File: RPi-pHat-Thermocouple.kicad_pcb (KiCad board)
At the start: 2 copper layers, 65 x 30 mm, 59 parts, among them J1 RPi_GPIO, J2 Barrel_Jack_Switch, P1 CONN_01X02, P2 CONN_01X02, P3 CONN_01X02, P6 CONN_01X03, Q1 NUD3124, Q2 BCM857BS, Q3 DMG2305UX, SW1 Write, U1 MAX31850K, U2 MAX31850K, U3 MAX31850K, U4 DS18S20, U5 AT24CS32, U6 LMZ21700, U7 MCP1754ST

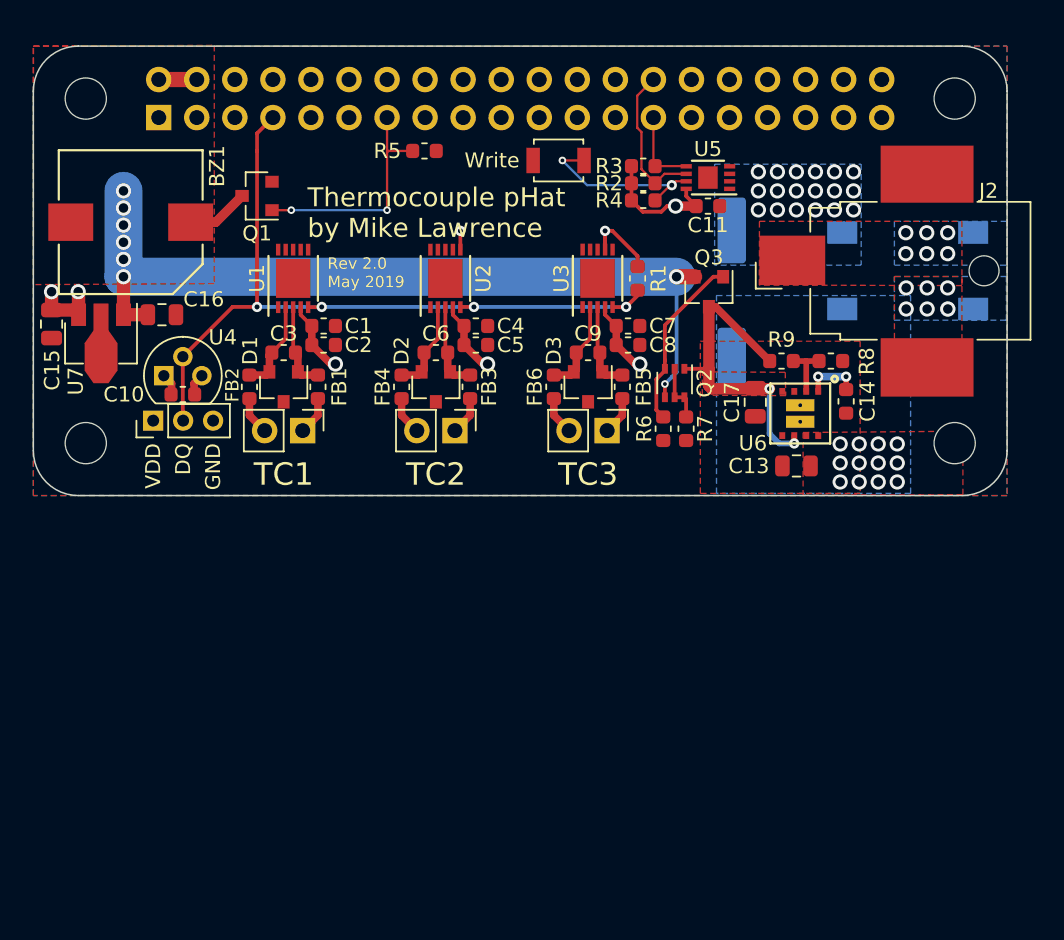
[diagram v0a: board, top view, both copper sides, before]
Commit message: Variation for generator monitoring application.
Remove buzzer and related; remove Pi Hat EEPROM.

Since the form factor is going to expand a bit beyond the Pi-Hat
specification to enable adding an isolated RS-232/TTL interface for
the Raspberry Pi serial port, we'll remove the parts that are not needed
for the generator-targeted application.
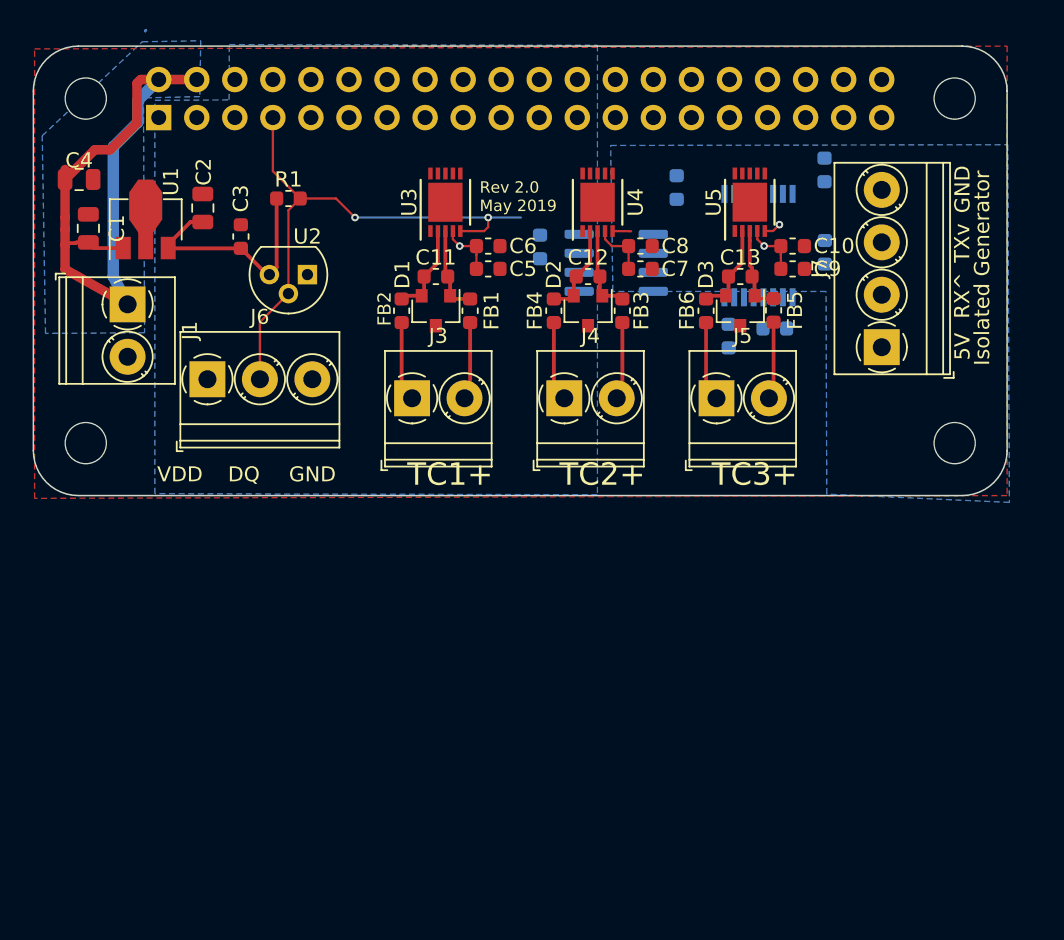
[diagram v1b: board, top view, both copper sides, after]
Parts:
- removed BZ1: Buzzer, Buzzer_Beeper-ML:MagneticBuzzer_CUI-CMI-9655S
- removed the C11 at (57.5, 35.2)
- removed the C12 at (59.1, 41.1)
- removed the C13 at (63.4, 52.5)
- removed D4: D_Bridge_+-AA, Diode_SMD:Diode_Bridge_Vishay_DFS
- removed the J2 at (69.0, 39.5)
- removed P1, P2, P3: CONN_01X02, Pin_Headers:Pin_Header_Straight_1x02_Pitch2.54mm
- removed P6: CONN_01X03, Pin_Headers:Pin_Header_Straight_1x03_Pitch2.00mm
- removed Q1: NUD3124, Package_TO_SOT_SMD:SOT-23
- removed Q2: BCM857BS, Package_TO_SOT_SMD:SOT-363_SC-70-6
- removed Q3: DMG2305UX, Package_TO_SOT_SMD:SOT-23
- removed R2, R3: 3.9k, Resistor_SMD:R_0603_1608Metric
- removed R4: 1k, Resistor_SMD:R_0603_1608Metric
- removed R5: 4.7k, Resistor_SMD:R_0603_1608Metric
- removed R6: 47k, Resistor_SMD:R_0603_1608Metric
- removed R7: 10k, Resistor_SMD:R_0603_1608Metric
- removed R8: 44.2k, Resistor_SMD:R_0603_1608Metric
- removed R9: 232k, Resistor_SMD:R_0603_1608Metric
- removed REF***: OSHW-Logo2_7.3x6mm_SilkScreen, Symbols:OSHW-Logo2_7.3x6mm_SilkScreen
- removed SW1: Write, Button_Switch_SMD:SW_SPST_B3U-1000P
- removed the U5 at (57.5, 33.3)
- added C15: 0.33uF, Capacitor_SMD:C_0603_1608Metric, B.Cu at (55.4, 33.9)
- added C16: 0.33uF, Capacitor_SMD:C_0603_1608Metric, B.Cu at (65.3, 38.3)
- added C17: 0.33uF, Capacitor_SMD:C_0603_1608Metric, B.Cu at (58.9, 43.9)
- added C18: 0.01uF, Capacitor_SMD:C_0603_1608Metric, B.Cu at (65.3, 32.8)
- added C19: 0.01uF, Capacitor_SMD:C_0603_1608Metric, B.Cu at (46.3, 37.9)
- added J1: Screw_Terminal_01x02, TerminalBlock_Phoenix:TerminalBlock_Phoenix_PT-1,5-2-3.5-H_1x02_P3.50mm_Horizontal, F.Cu at (18.8, 41.7)
- added J3: Screw_Terminal_01x02, TerminalBlock_Phoenix:TerminalBlock_Phoenix_PT-1,5-2-3.5-H_1x02_P3.50mm_Horizontal, F.Cu at (37.8, 48.0)
- added J4: Screw_Terminal_01x02, TerminalBlock_Phoenix:TerminalBlock_Phoenix_PT-1,5-2-3.5-H_1x02_P3.50mm_Horizontal, F.Cu at (47.9, 48.0)
- added J5: Screw_Terminal_01x02, TerminalBlock_Phoenix:TerminalBlock_Phoenix_PT-1,5-2-3.5-H_1x02_P3.50mm_Horizontal, F.Cu at (58.1, 48.0)
- added J6: Screw_Terminal_01x03, TerminalBlock_Phoenix:TerminalBlock_Phoenix_PT-1,5-3-3.5-H_1x03_P3.50mm_Horizontal, F.Cu at (24.1, 46.7)
- added J7: Screw_Terminal_01x04, TerminalBlock_Phoenix:TerminalBlock_Phoenix_PT-1,5-4-3.5-H_1x04_P3.50mm_Horizontal, F.Cu at (69.1, 44.6)
- added U7: ADuM1201ARZ, Package_SO:SOIC-8_3.9x4.9mm_P1.27mm, B.Cu at (51.4, 39.0)
- C14: value 3.3nF -> 0.047uF; moved to B.Cu
- C5: renamed from C2; value 10nF -> 0.01uF
- C7: renamed from C5; value 10nF -> 0.01uF
- C9: renamed from C8; value 10nF -> 0.01uF
- U6: value LMZ21700 -> MAX3221CDBR; footprint Converter_DCDC-ML:Converter_DCDC_Texas-SIL0008E -> Package_SO:SSOP-16_5.3x6.2mm_P0.65mm; moved to B.Cu
- moved C4 47.5 mm to (15.6, 33.4), turned to 0 degrees
- moved R1 23.9 mm to (29.5, 34.7), turned to 180 degrees
- moved C2 12.7 mm to (23.8, 35.3), turned to 270 degrees
- moved C8 12.2 mm to (53.0, 37.8)
- moved C6 12.2 mm to (42.9, 37.8)
- moved C10 12.2 mm to (63.2, 37.8)
- moved C7 12.1 mm to (53.0, 39.4)
- moved C5 12.1 mm to (42.9, 39.4)
- moved C9 12.1 mm to (63.2, 39.4)
- moved U2 11.7 mm to (30.8, 39.8), turned to 180 degrees
- moved U6 11.5 mm to (60.9, 37.8), turned to 90 degrees
- moved U3 11.4 mm to (40.0, 34.9)
- moved C12 11.4 mm to (49.5, 39.9)
- moved D2 11.4 mm to (49.5, 42.2)
- moved FB2 11.4 mm to (37.1, 42.2)
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- gave numbers to parts that had none: 4
- renumbered C16 to C1, C7 to C10, C3 to C11, C6 to C12, C9 to C13, C15 to C2, C10 to C3, C17 to C4, C1 to C6, C4 to C8, J1 to J2, U7 to U1, U4 to U2, U1 to U3, U2 to U4, U3 to U5
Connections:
- C14 pad 2: GND -> Net-(C14-Pad2)
- C4 pad 1: /+5VB -> +5V
- J2 pad 1: (no net) -> Net-(J2-Pad1)
- J2 pad 10: (no net) -> /RXD
- J2 pad 11: (no net) -> Net-(J2-Pad11)
- J2 pad 12: (no net) -> Net-(J2-Pad12)
- J2 pad 13: /ALERT -> Net-(J2-Pad13)
- J2 pad 15: (no net) -> Net-(J2-Pad15)
- J2 pad 16: (no net) -> Net-(J2-Pad16)
- J2 pad 17: (no net) -> Net-(J2-Pad17)
- J2 pad 18: (no net) -> Net-(J2-Pad18)
- J2 pad 19: (no net) -> Net-(J2-Pad19)
- J2 pad 21: (no net) -> Net-(J2-Pad21)
- J2 pad 22: (no net) -> Net-(J2-Pad22)
- J2 pad 23: (no net) -> Net-(J2-Pad23)
- J2 pad 24: (no net) -> Net-(J2-Pad24)
- J2 pad 26: (no net) -> Net-(J2-Pad26)
- J2 pad 27: /ID_SD -> Net-(J2-Pad27)
- J2 pad 28: /ID_SC -> Net-(J2-Pad28)
- J2 pad 29: (no net) -> Net-(J2-Pad29)
- J2 pad 3: (no net) -> Net-(J2-Pad3)
- J2 pad 31: (no net) -> Net-(J2-Pad31)
- J2 pad 32: (no net) -> Net-(J2-Pad32)
- J2 pad 33: (no net) -> Net-(J2-Pad33)
- J2 pad 35: (no net) -> Net-(J2-Pad35)
- J2 pad 36: (no net) -> Net-(J2-Pad36)
- J2 pad 37: (no net) -> Net-(J2-Pad37)
- J2 pad 38: (no net) -> Net-(J2-Pad38)
- J2 pad 40: (no net) -> Net-(J2-Pad40)
- J2 pad 5: (no net) -> Net-(J2-Pad5)
- J2 pad 8: (no net) -> /TXD
- U6 pad 1: Net-(C14-Pad1) -> /GENGND
- U6 pad 10: GND -> /GENGND
- U6 pad 2: Net-(R8-Pad1) -> Net-(C14-Pad1)
- U6 pad 3: (no net) -> Net-(C16-Pad1)
- U6 pad 4: /+5VB -> Net-(C14-Pad2)
- U6 pad 5: GND -> Net-(C15-Pad1)
- U6 pad 6: /+5VB -> Net-(C15-Pad2)
- U6 pad 7: /VBulk -> Net-(C17-Pad1)
- U6 pad 8: /VBulk -> Net-(U6-Pad8)
- U6 pad 9: GND -> /GENOUT
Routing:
- net /+5VB: track 22.1 -> 0.00 mm, vias 2 -> 0
- net /ALERT: track 15.6 -> 0.00 mm, vias 2 -> 0
- net +5V: track 59.2 -> 45.2 mm, vias 8 -> 0
- net /W1: track 52.5 -> 39.6 mm, vias 4 -> 3
- net Net-(R4-Pad2): track 12.0 -> 0.00 mm, vias 2 -> 0
- net Net-(Q2-Pad3): track 11.8 -> 0.00 mm
- net /ID_SC: track 10.2 -> 0.00 mm
- net +3.3VA: track 36.7 -> 27.7 mm, vias 8 -> 2
- net /ID_SD: track 5.41 -> 0.00 mm
- net Net-(BZ1-Pad2): track 4.16 -> 0.00 mm
- net Net-(Q2-Pad2): track 3.91 -> 0.00 mm
- net Net-(R8-Pad1): track 3.78 -> 0.00 mm
- net Net-(C14-Pad1): track 3.62 -> 0.00 mm, vias 2 -> 0
- net /TC2-: track 2.55 -> 5.34 mm
- net /TC3-: track 2.55 -> 5.34 mm
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- added copper zone on B.Cu, net +5V
- added copper zone on B.Cu, net /GENGND
- removed copper zone on F.Cu, net +5V
- removed copper zone on F.Cu, net /+5VB
- removed copper zone on B.Cu, net /AC1
- removed copper zone on F.Cu, net /AC1
- removed copper zone on B.Cu, net /AC2
- removed copper zone on F.Cu, net /AC2
- removed copper zone on B.Cu, net /VBulk
- removed copper zone on F.Cu, net /VBulk
- removed copper zone on B.Cu, net GND
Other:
- board text added: "5V"
- board text added: "Isolated Generator"
- board text added: "RX^"
- board text added: "TC1+"
- board text added: "TC2+"
- board text added: "TC3+"
- board text added: "TXv"

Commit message: PCB Version 3.0 files
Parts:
- added C20: 2.2uF, Capacitor_SMD:C_0805_2012Metric, F.Cu at (64.8, 60.1)
- added C21: 2.2uF, Capacitor_SMD:C_0805_2012Metric, F.Cu at (64.8, 50.4)
- added F1: Polyfuse 1206L010/60WR 0.1A, Fuse:Fuse_1206_3216Metric_Pad1.42x1.75mm_HandSolder, F.Cu at (54.9, 61.6)
- added J8: Conn_02x06_Odd_Even, Connector_PinHeader_2.54mm:PinHeader_2x06_P2.54mm_Vertical, F.Cu at (32.3, 38.0)
- added U8: MCP1754ST, Package_TO_SOT_SMD:SOT-89-3, F.Cu at (65.2, 55.7)
- added h5: , RPi_Hat:RPi_Hat_Mounting_Hole, F.Cu at (74.0, 77.0)
- added h6: , RPi_Hat:RPi_Hat_Mounting_Hole, F.Cu at (16.0, 77.0)
- C14, C15, C16, C17, C18, C19, U6: moved to F.Cu
- U3: value MAX31850K -> MAX31850KATB
- U4, U5: value MAX31850K -> MAX31850KATB+T
- U7: value ADuM1201ARZ -> ADuM1201ARZ-RL7; moved to F.Cu
- moved R1 35.3 mm to (56.9, 56.9)
- moved J6 34.8 mm to (51.3, 68.5)
- moved J1 26.8 mm to (19.3, 68.5), turned to 0 degrees
- moved J5 25.3 mm to (43.3, 68.5)
- moved J7 24.4 mm to (64.5, 68.5), turned to 0 degrees
- moved J4 24.1 mm to (35.3, 68.5)
- moved D1 23.7 mm to (26.6, 62.1)
- moved FB2 23.5 mm to (24.3, 61.9)
- moved FB1 23.5 mm to (28.8, 61.9)
- moved D2 23.4 mm to (36.4, 61.5)
- moved FB3 23.4 mm to (38.6, 61.5)
- moved FB4 23.4 mm to (34.1, 61.5)
- moved J3 23.1 mm to (27.3, 68.5)
- moved FB5 23.0 mm to (49.2, 61.4)
- moved FB6 23.0 mm to (44.7, 61.4)
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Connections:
- net /GENGND renamed Net-(C18-Pad2)
- C16 pad 2: /GEN5V -> /GEN3V3
- C17 pad 2: /GEN5V -> /GEN3V3
- C18 pad 1: /GEN5V -> /GEN3V3
- J2 pad 16: Net-(J2-Pad16) -> GPIO23
- J2 pad 18: Net-(J2-Pad18) -> GPIO24
- J2 pad 21: Net-(J2-Pad21) -> /GPIO9
- J2 pad 22: Net-(J2-Pad22) -> GPIO25
- J2 pad 24: Net-(J2-Pad24) -> GPIO8
- J2 pad 26: Net-(J2-Pad26) -> GPIO7
- J6 pad 1: +3.3VA -> Net-(F1-Pad1)
- U6 pad 12: /GEN5V -> /GEN3V3
- U6 pad 15: /GEN5V -> /GEN3V3
- U6 pad 16: /GEN5V -> /GEN3V3
- U7 pad 1: /GEN5V -> /GEN3V3
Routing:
- net /GEN3V3: track 0.00 -> 56.1 mm, vias 0 -> 2
- net /W1: track 39.6 -> 91.2 mm, vias 3 -> 0
- net +3.3VA: track 27.7 -> 66.2 mm, vias 2 -> 6
- net GND: track 0.00 -> 35.7 mm, vias 0 -> 3
- net /TXD: track 0.00 -> 31.7 mm
- net /GENIN: track 0.62 -> 32.1 mm
- net /GENOUT: track 0.00 -> 30.1 mm
- net /RXD: track 0.00 -> 29.3 mm
- net Net-(U6-Pad13): track 0.00 -> 25.8 mm
- net Net-(C18-Pad2): track 0.00 -> 23.7 mm, vias 0 -> 7
- net Net-(U6-Pad8): track 0.00 -> 23.5 mm
- net +5V: track 45.2 -> 31.5 mm, vias 0 -> 6
- net GPIO25: track 0.00 -> 13.6 mm
- net GPIO8: track 0.00 -> 13.5 mm
- net /GEN5V: track 0.00 -> 12.2 mm
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- added copper zone on B.Cu, net /GEN5V
- added copper zone on F.Cu, net Net-(C18-Pad2)
- removed copper zone on B.Cu, net Net-(C18-Pad2)
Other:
- board size 65 x 30 mm -> 65 x 56 mm
- board text added: "+ -"
- board text added: "+3.3V"
- board text added: "+5DC to Raspberry Pi"
- board text added: "+5V IN"
- board text added: "- +"
- board text added: "1-Wire Bus"
- board text added: "23"
- board text added: "24"
- board text added: "25"
- board text added: "3.3V out (fused)"
- board text added: "3.3V out fused"
- board text added: "7"
- board text added: "8"
- board text added: "9"
- board text added: "GND TX RX +5 Isolated Generator Controller Signals"
- board text added: "GPIO#"
- board text added: "Generator (Isolated)"
- board text added: "Generator Controller Isolated +5V"
- board text added: "Generator power supply and RS-232 signals isolated from Raspberry Pi and power supply. Do not interconnect generator ground and power supply with Raspberry Pi power to preserve galvanic isolation from controller and avoid ground loops."
- board text added: "Louis Mamakos"
- board text added: "RX in"
- board text added: "Rev 3.0 April 2020"
- board text added: "TX out"
- board text added: "Thermocouple Hat by Louis Mamakos (based on a design by Mike Lawrence)"
- board text added: "Type K Thermocouple Connections"
- board text added: "^ External DS18B20 temperature sensor connection."
- board text added: "https://www.transsys.com/posts/genmon-board/"
- board text removed: "DQ"
- board text removed: "Isolated Generator"
- board text removed: "RX^"
- board text removed: "Rev 2.0 May 2019"
- board text removed: "TC1+"
- board text removed: "TC2+"
- board text removed: "TC3+"
- board text removed: "TXv"
- board text removed: "Thermocouple pHat by Mike Lawrence"
- board text removed: "VDD"

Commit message: Candidate files for Version 3.1 of the PCB
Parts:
- added D20: ASMT-RF45-AN002, LED_SMD:LED_0603_1608Metric, F.Cu at (63.0, 41.8)
- added D21: NSR20F30NXT5G, Diode_SMD:D_0603_1608Metric, F.Cu at (65.0, 63.5)
- added D5: ASMT-RF45-AN002, LED_SMD:LED_0603_1608Metric, F.Cu at (21.5, 53.5)
- added J9: Conn_01x04_Male, Connector_PinHeader_2.54mm:PinHeader_1x04_P2.54mm_Vertical, F.Cu at (20.8, 38.1)
- added JP1: Jumper_NC_Small, Jumper:SolderJumper-2_P1.3mm_Bridged_RoundedPad1.0x1.5mm, B.Cu at (29.0, 34.5)
- added JP2: Jumper_NC_Small, Jumper:SolderJumper-2_P1.3mm_Bridged_RoundedPad1.0x1.5mm, B.Cu at (26.0, 34.5)
- added R10: 120, Resistor_SMD:R_0603_1608Metric, F.Cu at (23.5, 49.5)
- added R2: 330, Resistor_SMD:R_0603_1608Metric, F.Cu at (33.6, 34.0)
- added R20: 120, Resistor_SMD:R_0603_1608Metric, F.Cu at (65.0, 49.5)
- added R3: 330, Resistor_SMD:R_0603_1608Metric, F.Cu at (36.2, 34.0)
- added R4: 330, Resistor_SMD:R_0603_1608Metric, F.Cu at (38.6, 34.0)
- added R5: 330, Resistor_SMD:R_0603_1608Metric, F.Cu at (41.2, 34.0)
- added R6: 330, Resistor_SMD:R_0603_1608Metric, F.Cu at (43.8, 34.0)
- added R7: 330, Resistor_SMD:R_0603_1608Metric, F.Cu at (46.2, 34.0)
- added R8: 4.7k, Resistor_SMD:R_0603_1608Metric, F.Cu at (29.0, 33.9)
- added R9: 4.7k, Resistor_SMD:R_0603_1608Metric, F.Cu at (23.7, 32.1)
- C14: value 0.047uF -> 0.1uF
- C15, C16, C17: value 0.33uF -> 0.1uF
- U2: value DS18S20 -> DS18B20
- U3: value MAX31850KATB -> MAX31850KATB
- U4, U5: value MAX31850KATB+T -> MAX31850KATB
- U7: value ADuM1201ARZ-RL7 -> ADuM1201AR
- moved C17 10.8 mm to (74.1, 39.9), turned to 90 degrees
- moved C16 8.39 mm to (66.0, 45.1), turned to 270 degrees
- moved C4 7.90 mm to (15.5, 33.2), turned to 180 degrees
- moved C15 6.40 mm to (69.5, 44.1), turned to 0 degrees
- moved C14 5.35 mm to (74.1, 35.6), turned to 270 degrees
- moved J8 2.95 mm to (33.6, 40.6)
- moved U6 2.80 mm to (68.5, 37.9), turned to 90 degrees
- moved C21 1.65 mm to (65.0, 52.0)
- moved U8 1.08 mm to (66.3, 55.7)
- moved C7 0.73 mm to (40.5, 58.3)
- moved C8 0.68 mm to (40.5, 56.7)
- moved C5 0.53 mm to (30.0, 58.6)
- moved FB5 0.45 mm to (49.6, 61.2)
- moved FB4 0.43 mm to (33.7, 61.3)
- moved FB3 0.41 mm to (39.0, 61.3)
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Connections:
- net /GEN3V3 renamed +3V3
- net /RXD renamed Net-(J2-Pad10)
- net Net-(C18-Pad2) renamed GNDD
- net Net-(F1-Pad1) renamed /3V3FUSED
- J2 pad 3: Net-(J2-Pad3) -> /SDA
- J2 pad 5: Net-(J2-Pad5) -> /SCL
- J7 pad 1: /GEN5V -> Net-(D21-Pad2)
- J8 pad 10: /GPIO9 -> Net-(J8-Pad10)
- J8 pad 12: GPIO7 -> Net-(J8-Pad12)
- J8 pad 2: GPIO23 -> Net-(J8-Pad2)
- J8 pad 4: GPIO24 -> Net-(J8-Pad4)
- J8 pad 6: GPIO25 -> Net-(J8-Pad6)
- J8 pad 8: GPIO8 -> Net-(J8-Pad8)
- U6 pad 11: /GENIN -> /GEN-OUT-TTL
- U6 pad 13: Net-(U6-Pad13) -> /GENOUT
- U6 pad 8: Net-(U6-Pad8) -> /GENIN
- U6 pad 9: /GENOUT -> /GEN-IN-TTL
- U7 pad 2: Net-(U6-Pad8) -> /GEN-OUT-TTL
- U7 pad 3: Net-(U6-Pad13) -> /GEN-IN-TTL
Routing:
- net /3V3FUSED: track 6.72 -> 63.3 mm
- net +3.3VA: track 66.2 -> 95.3 mm
- net Net-(U6-Pad13): track 25.8 -> 0.00 mm
- net +3V3: track 56.1 -> 30.9 mm, vias 2 -> 6
- net GNDD: track 23.7 -> 0.00 mm, vias 7 -> 0
- net Net-(U6-Pad8): track 23.5 -> 0.00 mm
- net /GEN-IN-TTL: track 0.00 -> 16.7 mm
- net /GEN-OUT-TTL: track 0.00 -> 14.3 mm
- net /SCL: track 0.00 -> 12.0 mm
- net /SDA: track 0.00 -> 9.86 mm
- net Net-(D20-Pad2): track 0.00 -> 7.40 mm
- net Net-(JP2-Pad1): track 0.00 -> 6.37 mm, vias 0 -> 1
- net Net-(C14-Pad1): track 4.49 -> 10.5 mm
- net /GENOUT: track 30.1 -> 35.9 mm, vias 0 -> 1
- net /W1: track 91.2 -> 96.9 mm
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- added copper zone on B.Cu, net +3V3
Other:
- board text added: "1"
- board text added: "3v3"
- board text added: "Cut links to disable I2C pull-ups"
- board text added: "Do not connect external power if Raspberry Pi is USB Powered"
- board text added: "GND TX RX +5 Isolated Generator Signals"
- board text added: "Gen PWR"
- board text added: "Generator Isolated +3.3V"
- board text added: "Gnd"
- board text added: "I2C expansion"
- board text added: "PWR"
- board text added: "Rev 3.1 April 2020"
- board text added: "SCL"
- board text added: "SCL PU"
- board text added: "SCL SDA 3v3 GND"
- board text added: "SDA"
- board text added: "SDA PU"
- board text added: "Thermocouple Hat by Louis Mamakos"
- board text added: "TransSys Internetworking LLC"
- board text added: "WARNING"
- board text added: "ext +5VDC"
- board text removed: "GND TX RX +5 Isolated Generator Controller Signals"
- board text removed: "Generator power supply and RS-232 signals isolated from Raspberry Pi and power supply. Do not interconnect generator ground and power supply with Raspberry Pi power to preserve galvanic isolation from controller and avoid ground loops."
- board text removed: "Rev 3.0 April 2020"
- board text removed: "Thermocouple Hat by Louis Mamakos (based on a design by Mike Lawrence)"
